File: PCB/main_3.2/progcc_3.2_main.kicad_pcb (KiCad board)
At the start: 4 copper layers, 110.9 x 59.7 mm, 140 parts, among them J1 Conn_01x04_Pin, J2 SM02B-SURS-TF_LF__SN_, J3 To Button Board, J4 SM02B-SURS-TF_LF__SN_, J5 Conn_01x02_Pin, J9 USB_C_Receptacle, Q1 MMBT2222A, Q2 MMBT2222A, Q4 BSS138DW, Q5 BSS138DW, Q7 MMBT3904, Q8 MMBT3904, SW1 GL1807SYAE-002, SW2 GL1807SYAE-002, SW3 1TS026A-1000-0550, SW4 TS35CA, SW5 1TS026A-1000-0550, T1 36-8730, T2 36-8730, T3 36-8730, T4 36-8730, U10 MCP3002, U11 ST_LSM6, U12 PI3USB4000A, U13 GD25Q80EEIGR, U14 TPS63001DRCR, U16 BQ25180, U5 ST_LSM6, U6 RP2040, U7 CH340K, U8 MCP3002, U9 ESP32-PICO-MINI-02, Y1 Crystal_GND3

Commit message: Update 3.2 PCB
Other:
- board text added: "ProGCC 3.2"
- board text removed: "ProGCC 3.2 r1"
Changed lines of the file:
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@@
 		(tags "capacitor")
 		(property "Reference" "C19"
-			(at 1.807294 0.0289 90)
+			(at -0.232506 2.6035 90)
 			(unlocked yes)
 			(layer "F.SilkS")
-			(hide yes)
 			(effects
 				(font
@@
 		(tags "capacitor")
 		(property "Reference" "C21"
-			(at 0.192706 -1.7445 90)
+			(at 0.816706 -2.4511 90)
 			(unlocked yes)
 			(layer "F.SilkS")
@@
 		)
 	)
-	(gr_text "ProGCC 3.2 r1"
+	(gr_text "ProGCC 3.2"
 		(at 159.893 122.7836 0)
 		(layer "F.SilkS")

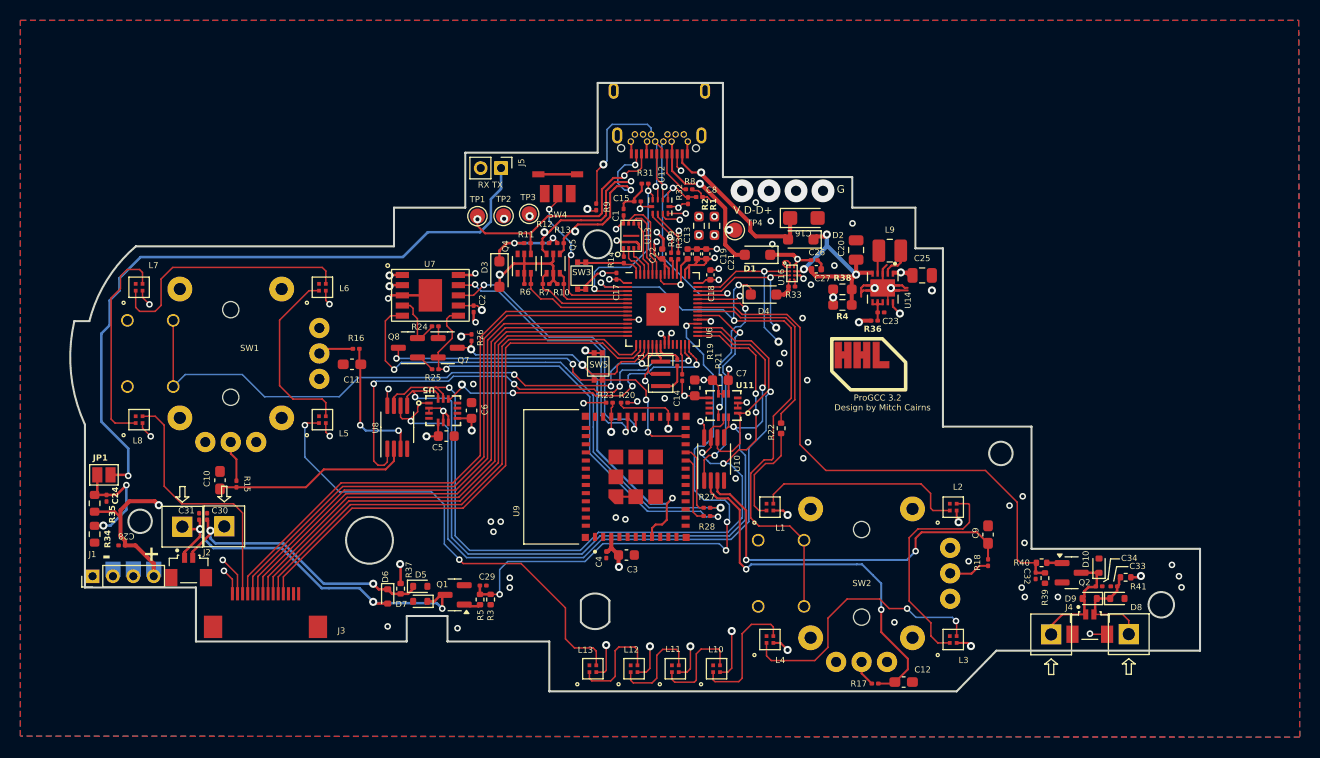
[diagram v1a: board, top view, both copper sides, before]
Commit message: Update PCB Files
- Standardize differing resistor sizes
- Update oscillator
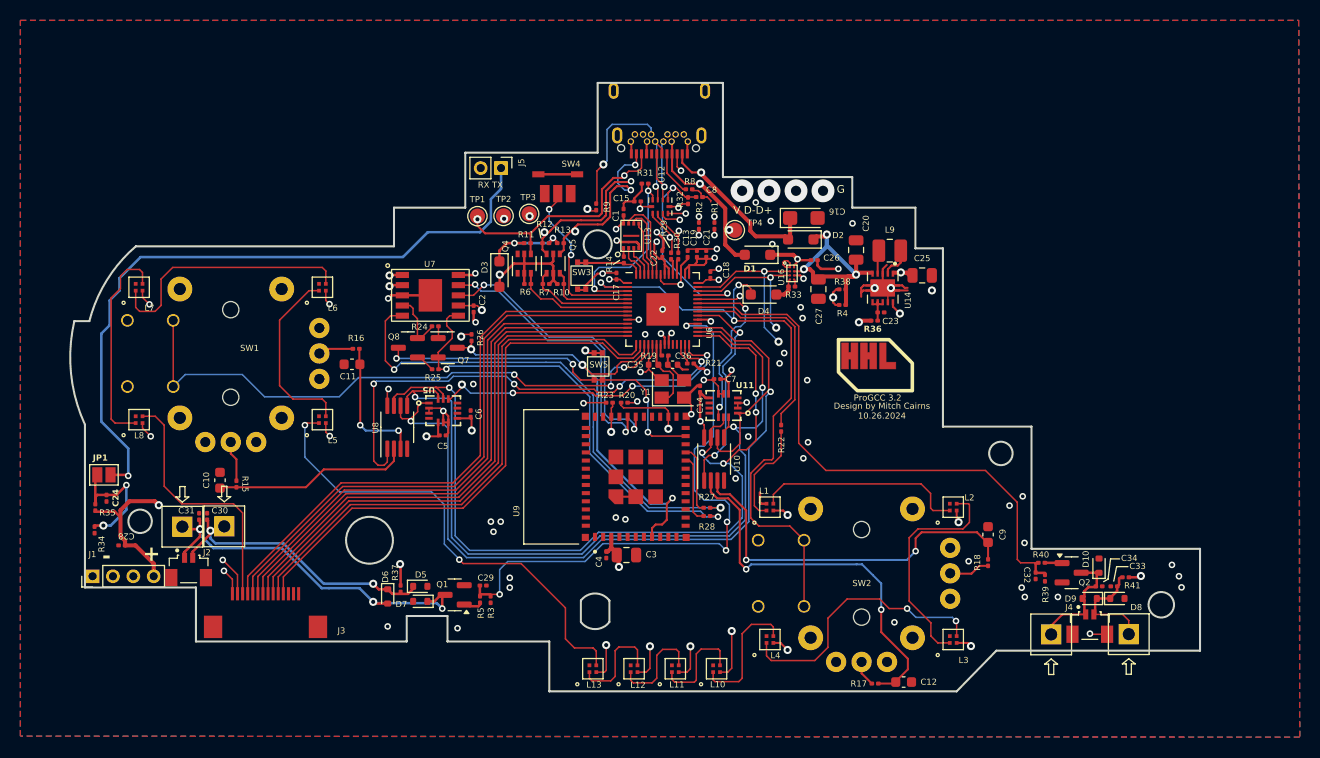
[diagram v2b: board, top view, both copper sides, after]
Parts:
- removed ? (x2): , 
- removed the REF** at (158.3, 119.9)
- removed the REF** at (84.8, 139.6)
- added C35: 15pF, Capacitor_SMD:C_0402_1005Metric, F.Cu at (137.9, 119.5)
- added C36: 15pF, Capacitor_SMD:C_0402_1005Metric, F.Cu at (139.8, 119.5)
- added REF**: HHL_Logo, hhl:HHL_Logo, F.Cu at (159.0, 120.0)
- C1, C15, C17, C2, C23, C24, C4: value 100n -> 100nF
- C10, C11, C12, C9: value .047u -> 47nF; footprint Capacitor_SMD:C_0603_1608Metric_Pad1.08x0.95mm_HandSolder -> Capacitor_SMD:C_0603_1608Metric
- C13, C18, C21, C22: value 100n -> 100nF; footprint Capacitor_SMD:C_0402_1005Metric -> Capacitor_SMD:C_0201_0603Metric
- C14, C5, C6, C7: footprint Capacitor_SMD:C_0603_1608Metric -> Capacitor_SMD:C_0201_0603Metric
- C16: value 47uF 6.3v -> 47uF
- C19: value 1u -> 1uF; footprint Capacitor_SMD:C_0402_1005Metric -> Capacitor_SMD:C_0201_0603Metric
- C26, C28, C30, C31, C33, C34, C8: value 1u -> 1uF
- C27: footprint Capacitor_SMD:C_0402_1005Metric -> Capacitor_SMD:C_0805_2012Metric
- C3: value 10uF/10V (20%) -> 10uF; footprint Capacitor_SMD:C_0603_1608Metric -> Capacitor_SMD:C_0805_2012Metric
- R1, R2, R38, R4: footprint Resistor_SMD:R_0603_1608Metric_Pad0.98x0.95mm_HandSolder -> Resistor_SMD:R_0201_0603Metric
- R22: value 330 -> 330R; footprint Resistor_SMD:R_0402_1005Metric -> Resistor_SMD:R_0201_0603Metric
- R27, R28: value 0 -> 0R
- R29, R30: value 27 -> 27R
- R3, R37, R39, R40, R41, R5: footprint Resistor_SMD:R_0402_1005Metric -> Resistor_SMD:R_0201_0603Metric
- R34, R35: footprint Resistor_SMD:R_0603_1608Metric -> Resistor_SMD:R_0201_0603Metric
- R36: value 100 -> 100R
- Y1: value Crystal_GND3 -> ABM8-272-T3; footprint Crystal:Resonator_SMD_Murata_CSTxExxV-3Pin_3.0x1.1mm -> Crystal:Crystal_SMD_3225-4Pin_3.2x2.5mm
- moved C27 1.97 mm to (154.1, 112.1), turned to 90 degrees
- moved Y1 1.90 mm to (139.8, 121.9), turned to 0 degrees
- moved R21 1.60 mm to (141.5, 119.4), turned to 180 degrees
- moved R19 1.39 mm to (139.0, 118.6), turned to 0 degrees
- moved C14 0.53 mm to (142.5, 121.9)
- moved R34 0.42 mm to (83.0, 135.8)
- moved R35 0.41 mm to (83.1, 133.5)
- moved C5 0.36 mm to (117.2, 126.5)
- moved C6 0.33 mm to (119.9, 124.4)
- moved C7 0.32 mm to (144.2, 121.0)
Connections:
- R19 pad 1: Net-(R19-Pad1) -> XTAL_OUT
- R19 pad 2: XTAL_OUT -> Net-(C36-Pad1)
- Y1 pad 3: Net-(R19-Pad1) -> Net-(C36-Pad1)
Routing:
- net GND: track 74.0 -> 83.5 mm, vias 57 -> 58
- net XTAL_IN: track 1.86 -> 7.21 mm
- net Net-(R19-Pad1): track 3.34 -> 0.00 mm
- net Net-(C36-Pad1): track 0.00 -> 3.31 mm
- net +3V3: track 103.1 -> 105.3 mm
- net LADC_CS: track 46.3 -> 48.0 mm
- net XTAL_OUT: track 2.78 -> 1.16 mm
- net BAT_LVL: track 87.6 -> 89.2 mm
- net LRA_L: track 57.0 -> 58.1 mm
- net IMU0_CS: track 30.3 -> 31.4 mm
- net /RUN: track 2.98 -> 2.13 mm
- net RP_USB+: track 7.72 -> 8.32 mm
- net RP_USB-: track 9.22 -> 9.81 mm
- net D-: track 23.5 -> 24.0 mm
- net D+: track 24.7 -> 25.3 mm
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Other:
- board text added: "Design by Mitch Cairns 10.26.2024"
- board text removed: "Design by Mitch Cairns"
